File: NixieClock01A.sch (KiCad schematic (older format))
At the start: 39 parts, among them J1 Conn_01x10, J13 Conn_02x18_Odd_Even, J14 Conn_01x08, J15 Conn_01x08, J2 Conn_01x08, J3 Conn_01x08, J4 Conn_01x08, J5 Conn_01x01_Male, J6 Conn_01x01_Male, J7 Conn_01x01_Male, J8 Conn_01x01_Male, Q1 Q_NMOS_GDS, U1 DS3231, U4 LM3478

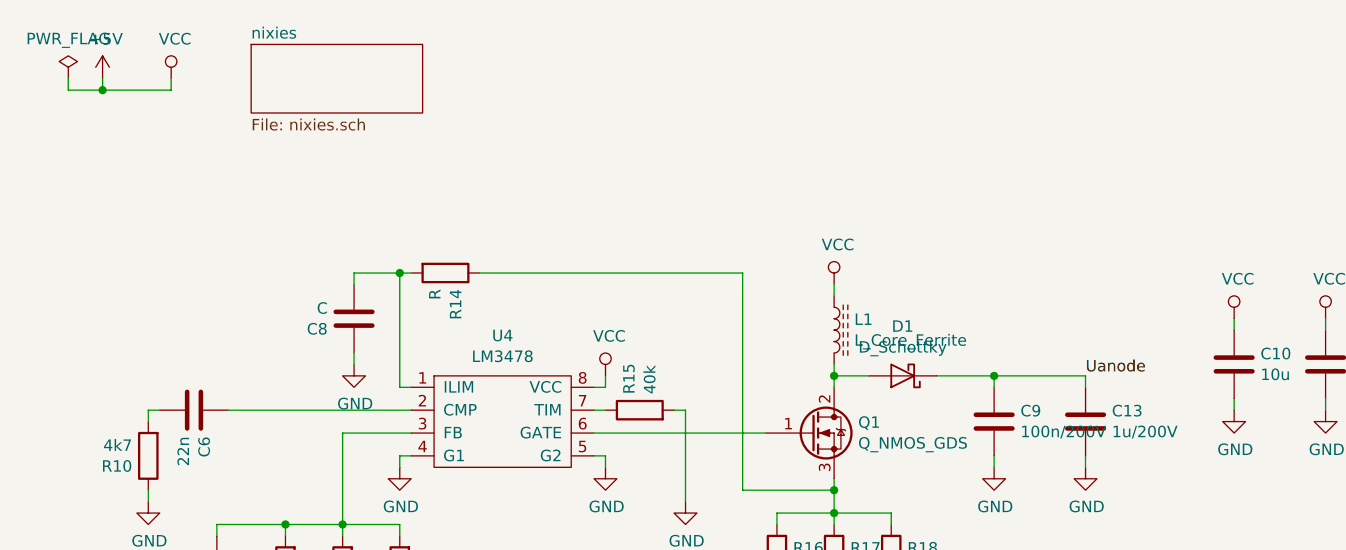
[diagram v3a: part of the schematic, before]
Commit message: Added all nixies, added DC-DC converter, basic routing done
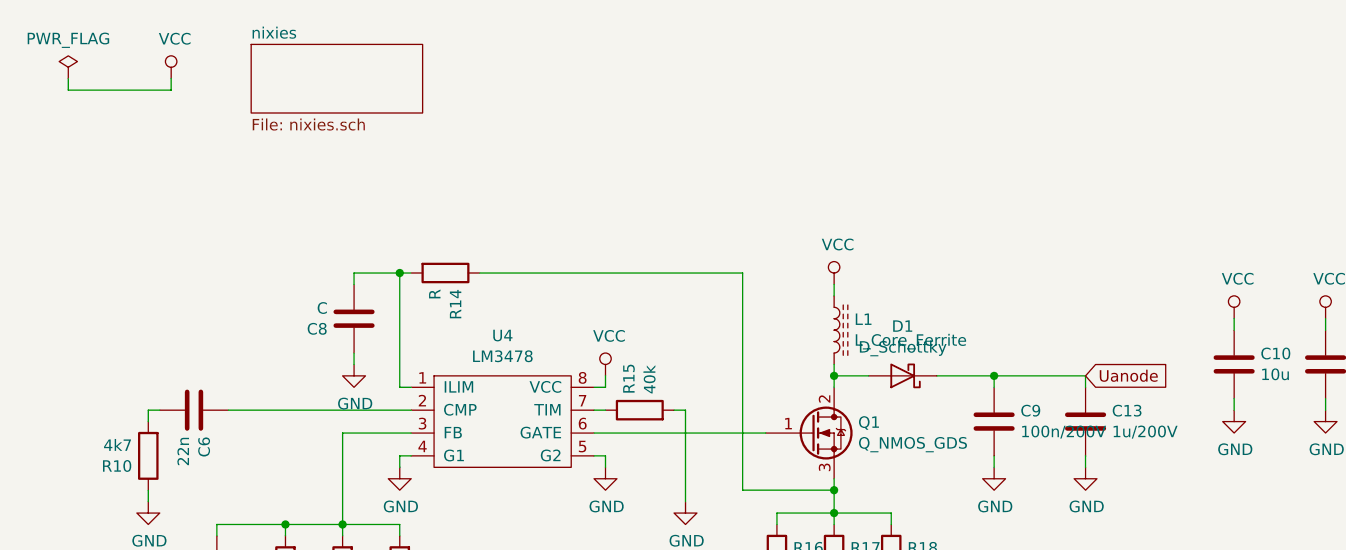
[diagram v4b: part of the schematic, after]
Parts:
- J1: footprint Connector_PinSocket_2.54mm:PinSocket_1x10_P2.54mm_Vertical -> Connector_PinHeader_2.54mm:PinHeader_1x10_P2.54mm_Vertical
- J14, J15, J2, J3, J4: footprint Connector_PinSocket_2.54mm:PinSocket_1x08_P2.54mm_Vertical -> Connector_PinHeader_2.54mm:PinHeader_1x08_P2.54mm_Vertical
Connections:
- wire segments 139 -> 137
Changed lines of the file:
@@
 Wire Wire Line
 	2500 2625 2500 2675
-Text Label 5500 2275 0    50   ~ 0
-Uanode
 Text Label 2550 3325 0    50   ~ 0
 Uanode
@@
 	10700 6025 10700 6075
 $Comp
-L power:+5V #PWR0202
-U 1 1 5B5AA1D2
-P 1200 975
-F 0 "#PWR0202" H 1200 825 50  0001 C CNN
-F 1 "+5V" H 1215 1148 50  0000 C CNN
-F 2 "" H 1200 975 50  0001 C CNN
-F 3 "" H 1200 975 50  0001 C CNN
-	1    1200 975
-	1    0    0    -1
-$EndComp
-$Comp
 L power:VCC #PWR0204
 U 1 1 5B5AA546
@@
 $EndComp
 Wire Wire Line
-	1200 975  1200 1025
-Wire Wire Line
-	1200 1025 1500 1025
-Wire Wire Line
 	1500 1025 1500 975
 $Comp
@@
 Wire Wire Line
 	1050 975  1050 1025
-Wire Wire Line
-	1050 1025 1200 1025
-Connection ~ 1200 1025
 Wire Wire Line
 	3350 2425 3400 2425
@@
 F 0 "J1" H 10580 1217 50  0000 L CNN
 F 1 "Conn_01x10" H 10580 1126 50  0000 L CNN
-F 2 "Connector_PinSocket_2.54mm:PinSocket_1x10_P2.54mm_Vertical" H 10500 1225 50  0001 C CNN
+F 2 "Connector_PinHeader_2.54mm:PinHeader_1x10_P2.54mm_Vertical" H 10500 1225 50  0001 C CNN
 F 3 "~" H 10500 1225 50  0001 C CNN
 	1    10500 1225
@@
 F 0 "J14" H 10580 2192 50  0000 L CNN
 F 1 "Conn_01x08" H 10580 2101 50  0000 L CNN
-F 2 "Connector_PinSocket_2.54mm:PinSocket_1x08_P2.54mm_Vertical" H 10500 2200 50  0001 C CNN
+F 2 "Connector_PinHeader_2.54mm:PinHeader_1x08_P2.54mm_Vertical" H 10500 2200 50  0001 C CNN
 F 3 "~" H 10500 2200 50  0001 C CNN
 	1    10500 2200
@@
 F 0 "J15" H 10580 3042 50  0000 L CNN
 F 1 "Conn_01x08" H 10580 2951 50  0000 L CNN
-F 2 "Connector_PinSocket_2.54mm:PinSocket_1x08_P2.54mm_Vertical" H 10500 3050 50  0001 C CNN
+F 2 "Connector_PinHeader_2.54mm:PinHeader_1x08_P2.54mm_Vertical" H 10500 3050 50  0001 C CNN
 F 3 "~" H 10500 3050 50  0001 C CNN
 	1    10500 3050
@@
 F 0 "J4" H 8980 3017 50  0000 L CNN
 F 1 "Conn_01x08" H 8980 2926 50  0000 L CNN
-F 2 "Connector_PinSocket_2.54mm:PinSocket_1x08_P2.54mm_Vertical" H 8900 3025 50  0001 C CNN
+F 2 "Connector_PinHeader_2.54mm:PinHeader_1x08_P2.54mm_Vertical" H 8900 3025 50  0001 C CNN
 F 3 "~" H 8900 3025 50  0001 C CNN
 	1    8900 3025
@@
 F 0 "J3" H 8980 2167 50  0000 L CNN
 F 1 "Conn_01x08" H 8980 2076 50  0000 L CNN
-F 2 "Connector_PinSocket_2.54mm:PinSocket_1x08_P2.54mm_Vertical" H 8900 2175 50  0001 C CNN
+F 2 "Connector_PinHeader_2.54mm:PinHeader_1x08_P2.54mm_Vertical" H 8900 2175 50  0001 C CNN
 F 3 "~" H 8900 2175 50  0001 C CNN
 	1    8900 2175
@@
 F 0 "J2" H 8980 1317 50  0000 L CNN
 F 1 "Conn_01x08" H 8980 1226 50  0000 L CNN
-F 2 "Connector_PinSocket_2.54mm:PinSocket_1x08_P2.54mm_Vertical" H 8900 1325 50  0001 C CNN
+F 2 "Connector_PinHeader_2.54mm:PinHeader_1x08_P2.54mm_Vertical" H 8900 1325 50  0001 C CNN
 F 3 "~" H 8900 1325 50  0001 C CNN
 	1    8900 1325
@@
 Text Notes 9650 2975 1    128  ~ 0
 Arduino Mega
+Wire Wire Line
+	1050 1025 1500 1025
+Text GLabel 5500 2275 2    50   Input ~ 0
+Uanode
 $EndSCHEMATC

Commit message: Added RTC, ERC done, DRC done, Silk layer revision
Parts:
- removed J5, J7: Conn_01x01_Male, MountingHole:MountingHole_3.2mm_M3_DIN965_Pad, symbol Connector:Conn_01x01_Male
- added C1: 100n, Capacitor_SMD:C_0603_1608Metric, symbol NixieClock01A-rescue:C-Device
- added R80, R81: 4k7, Resistor_SMD:R_0603_1608Metric, symbol NixieClock01A-rescue:R-Device
- added R82: 100k, Resistor_SMD:R_0603_1608Metric, symbol NixieClock01A-rescue:R-Device
- U1: footprint Housings_SOIC:SOIC-16_7.5x10.3mm_Pitch1.27mm -> Package_SO:SOIC-16W_7.5x10.3mm_P1.27mm
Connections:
- net labels removed: +3.3V, 14, 15, 16, 17, 18, 19, 2, 3, AREF, IOREF, RES, RX, TX
- wire segments 137 -> 154
- no-connect marks 1 -> 18
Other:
- moved on the sheet: C10, C12, C13, C14, C6, C7, C8, C9, D1, J1, J13, J14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

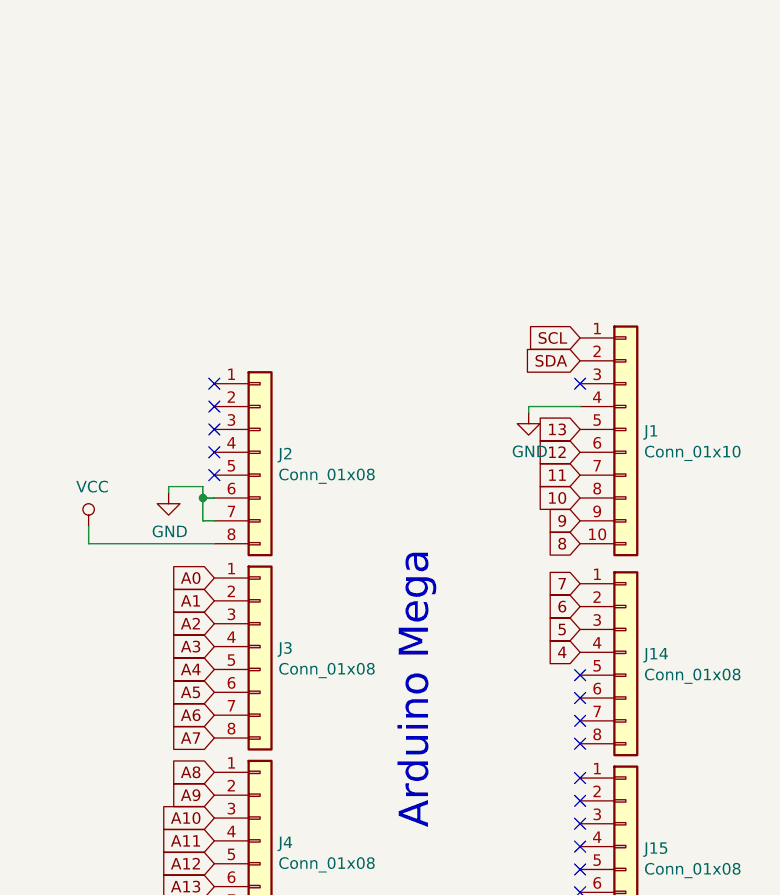
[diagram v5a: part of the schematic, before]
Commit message: Added buttons
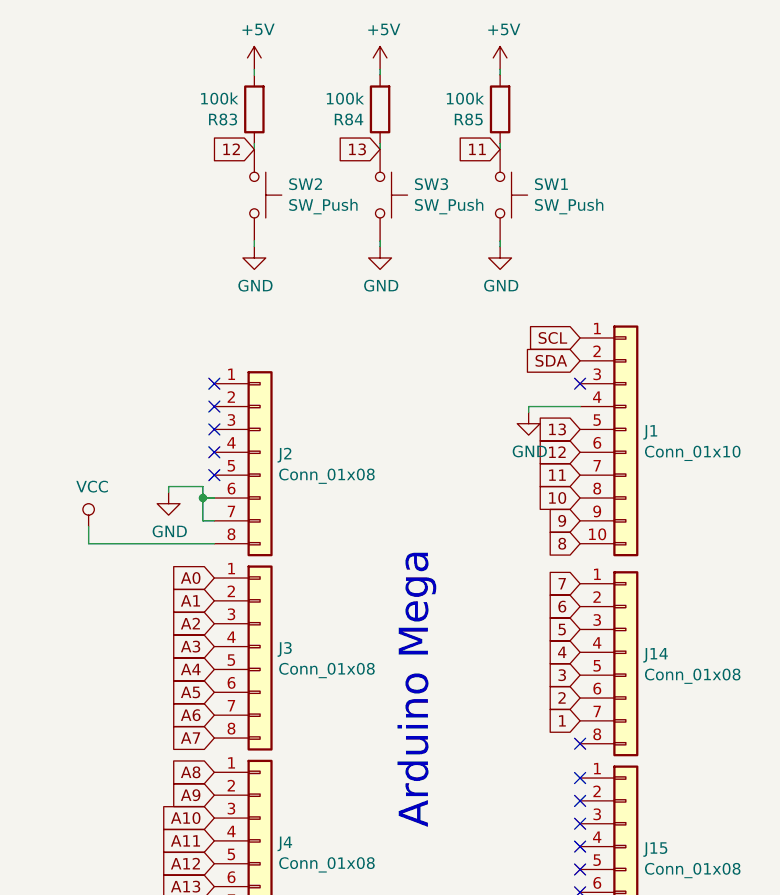
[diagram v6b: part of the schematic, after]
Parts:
- added R83, R84, R85: 100k, Resistor_SMD:R_0603_1608Metric, symbol NixieClock01A-rescue:R-Device
- added SW1, SW2, SW3: SW_Push, kicad-footprints-master:SMD-PushButton-6x3.6mm, symbol Switch:SW_Push
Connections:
- net +5V: now also R83.2, R84.2, R85.2
- net 11: now also R85.1, SW1.1
- net 12: now also R83.1, SW2.1
- net 13: now also R84.1, SW3.1
- net GND: now also SW1.2, SW2.2, SW3.2
- net 3: now reaches J14.5 (Pin_5)
- net 2: now reaches J14.6 (Pin_6)
- net 1: now reaches J14.7 (Pin_7)
- no-connect marks 18 -> 15
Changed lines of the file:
@@
 NoConn ~ 8775 2600
 NoConn ~ 8775 2700
-NoConn ~ 10375 3675
-NoConn ~ 10375 3775
-NoConn ~ 10375 3875
 NoConn ~ 10375 3975
 NoConn ~ 10375 4125
@@
 Wire Wire Line
 	1575 2075 1575 2050
+Text GLabel 10375 3675 0    50   Input ~ 0
+3
+Text GLabel 10375 3775 0    50   Input ~ 0
+2
+Text GLabel 10375 3875 0    50   Input ~ 0
+1
+$Comp
+L Switch:SW_Push SW1
+U 1 1 5C97920D
+P 10025 1575
+F 0 "SW1" V 9979 1723 50  0000 L CNN
+F 1 "SW_Push" V 10070 1723 50  0000 L CNN
+F 2 "kicad-footprints-master:SMD-PushButton-6x3.6mm" H 10025 1775 50  0001 C CNN
+F 3 "" H 10025 1775 50  0001 C CNN
+	1    10025 1575
+	0    1    1    0
+$EndComp
+$Comp
+L NixieClock01A-rescue:R-Device R85
+U 1 1 5C979D42
+P 10025 1200
+F 0 "R85" H 10095 1246 50  0000 L CNN
+F 1 "100k" H 10095 1155 50  0000 L CNN
+F 2 "Resistor_SMD:R_0603_1608Metric" V 9955 1200 50  0001 C CNN
+F 3 "~" H 10025 1200 50  0001 C CNN
+	1    10025 1200
+	-1   0    0    1
+$EndComp
+$Comp
+L power:+5V #PWR0136
+U 1 1 5C97A230
+P 10025 1025
+F 0 "#PWR0136" H 10025 875 50  0001 C CNN
+F 1 "+5V" H 10040 1198 50  0000 C CNN
+F 2 "" H 10025 1025 50  0001 C CNN
+F 3 "" H 10025 1025 50  0001 C CNN
+	1    10025 1025
+	1    0    0    -1
+$EndComp
+Wire Wire Line
+	10025 1025 10025 1050
+Wire Wire Line
+	10025 1350 10025 1375
+$Comp
+L power:GND #PWR0193
+U 1 1 5C986889
+P 10025 1800
+F 0 "#PWR0193" H 10025 1550 50  0001 C CNN
+F 1 "GND" H 10030 1627 50  0000 C CNN
+F 2 "" H 10025 1800 50  0001 C CNN
+F 3 "" H 10025 1800 50  0001 C CNN
+	1    10025 1800
+	1    0    0    -1
+$EndComp
+Wire Wire Line
+	10025 1800 10025 1775
+$Comp
+L Switch:SW_Push SW3
+U 1 1 5C98CE79
+P 9500 1575
+F 0 "SW3" V 9454 1723 50  0000 L CNN
+F 1 "SW_Push" V 9545 1723 50  0000 L CNN
+F 2 "kicad-footprints-master:SMD-PushButton-6x3.6mm" H 9500 1775 50  0001 C CNN
+F 3 "" H 9500 1775 50  0001 C CNN
+	1    9500 1575
+	0    1    1    0
+$EndComp
+$Comp
+L NixieClock01A-rescue:R-Device R84
+U 1 1 5C98CE7F
+P 9500 1200
+F 0 "R84" H 9570 1246 50  0000 L CNN
+F 1 "100k" H 9570 1155 50  0000 L CNN
+F 2 "Resistor_SMD:R_0603_1608Metric" V 9430 1200 50  0001 C CNN
+F 3 "~" H 9500 1200 50  0001 C CNN
+	1    9500 1200
+	-1   0    0    1
+$EndComp
+$Comp
+L power:+5V #PWR0194
+U 1 1 5C98CE85
+P 9500 1025
+F 0 "#PWR0194" H 9500 875 50  0001 C CNN
+F 1 "+5V" H 9515 1198 50  0000 C CNN
+F 2 "" H 9500 1025 50  0001 C CNN
+F 3 "" H 9500 1025 50  0001 C CNN
+	1    9500 1025
+	1    0    0    -1
+$EndComp
+Wire Wire Line
+	9500 1025 9500 1050
+Wire Wire Line
+	9500 1350 9500 1375
+$Comp
+L power:GND #PWR0196
+U 1 1 5C98CE8D
+P 9500 1800
+F 0 "#PWR0196" H 9500 1550 50  0001 C CNN
+F 1 "GND" H 9505 1627 50  0000 C CNN
+F 2 "" H 9500 1800 50  0001 C CNN
+F 3 "" H 9500 1800 50  0001 C CNN
+	1    9500 1800
+	1    0    0    -1
+$EndComp
+Wire Wire Line
+	9500 1800 9500 1775
+$Comp
+L Switch:SW_Push SW2
+U 1 1 5C993582
+P 8950 1575
+F 0 "SW2" V 8904 1723 50  0000 L CNN
+F 1 "SW_Push" V 8995 1723 50  0000 L CNN
+F 2 "kicad-footprints-master:SMD-PushButton-6x3.6mm" H 8950 1775 50  0001 C CNN
+F 3 "" H 8950 1775 50  0001 C CNN
+	1    8950 1575
+	0    1    1    0
+$EndComp
+$Comp
+L NixieClock01A-rescue:R-Device R83
+U 1 1 5C993588
+P 8950 1200
+F 0 "R83" H 9020 1246 50  0000 L CNN
+F 1 "100k" H 9020 1155 50  0000 L CNN
+F 2 "Resistor_SMD:R_0603_1608Metric" V 8880 1200 50  0001 C CNN
+F 3 "~" H 8950 1200 50  0001 C CNN
+	1    8950 1200
+	-1   0    0    1
+$EndComp
+$Comp
+L power:+5V #PWR0197
+U 1 1 5C99358E
+P 8950 1025
+F 0 "#PWR0197" H 8950 875 50  0001 C CNN
+F 1 "+5V" H 8965 1198 50  0000 C CNN
+F 2 "" H 8950 1025 50  0001 C CNN
+F 3 "" H 8950 1025 50  0001 C CNN
+	1    8950 1025
+	1    0    0    -1
+$EndComp
+Wire Wire Line
+	8950 1025 8950 1050
+Wire Wire Line
+	8950 1350 8950 1375
+$Comp
+L power:GND #PWR0198
+U 1 1 5C993596
+P 8950 1800
+F 0 "#PWR0198" H 8950 1550 50  0001 C CNN
+F 1 "GND" H 8955 1627 50  0000 C CNN
+F 2 "" H 8950 1800 50  0001 C CNN
+F 3 "" H 8950 1800 50  0001 C CNN
+	1    8950 1800
+	1    0    0    -1
+$EndComp
+Wire Wire Line
+	8950 1800 8950 1775
+Text GLabel 9500 1375 0    50   Input ~ 0
+13
+Text GLabel 8950 1375 0    50   Input ~ 0
+12
+Text GLabel 10025 1375 0    50   Input ~ 0
+11
 $EndSCHEMATC
